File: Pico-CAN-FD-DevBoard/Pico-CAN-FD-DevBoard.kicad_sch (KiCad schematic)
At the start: 2 parts, among them U1 RP2350A, U2 MCP251863T-H-SS

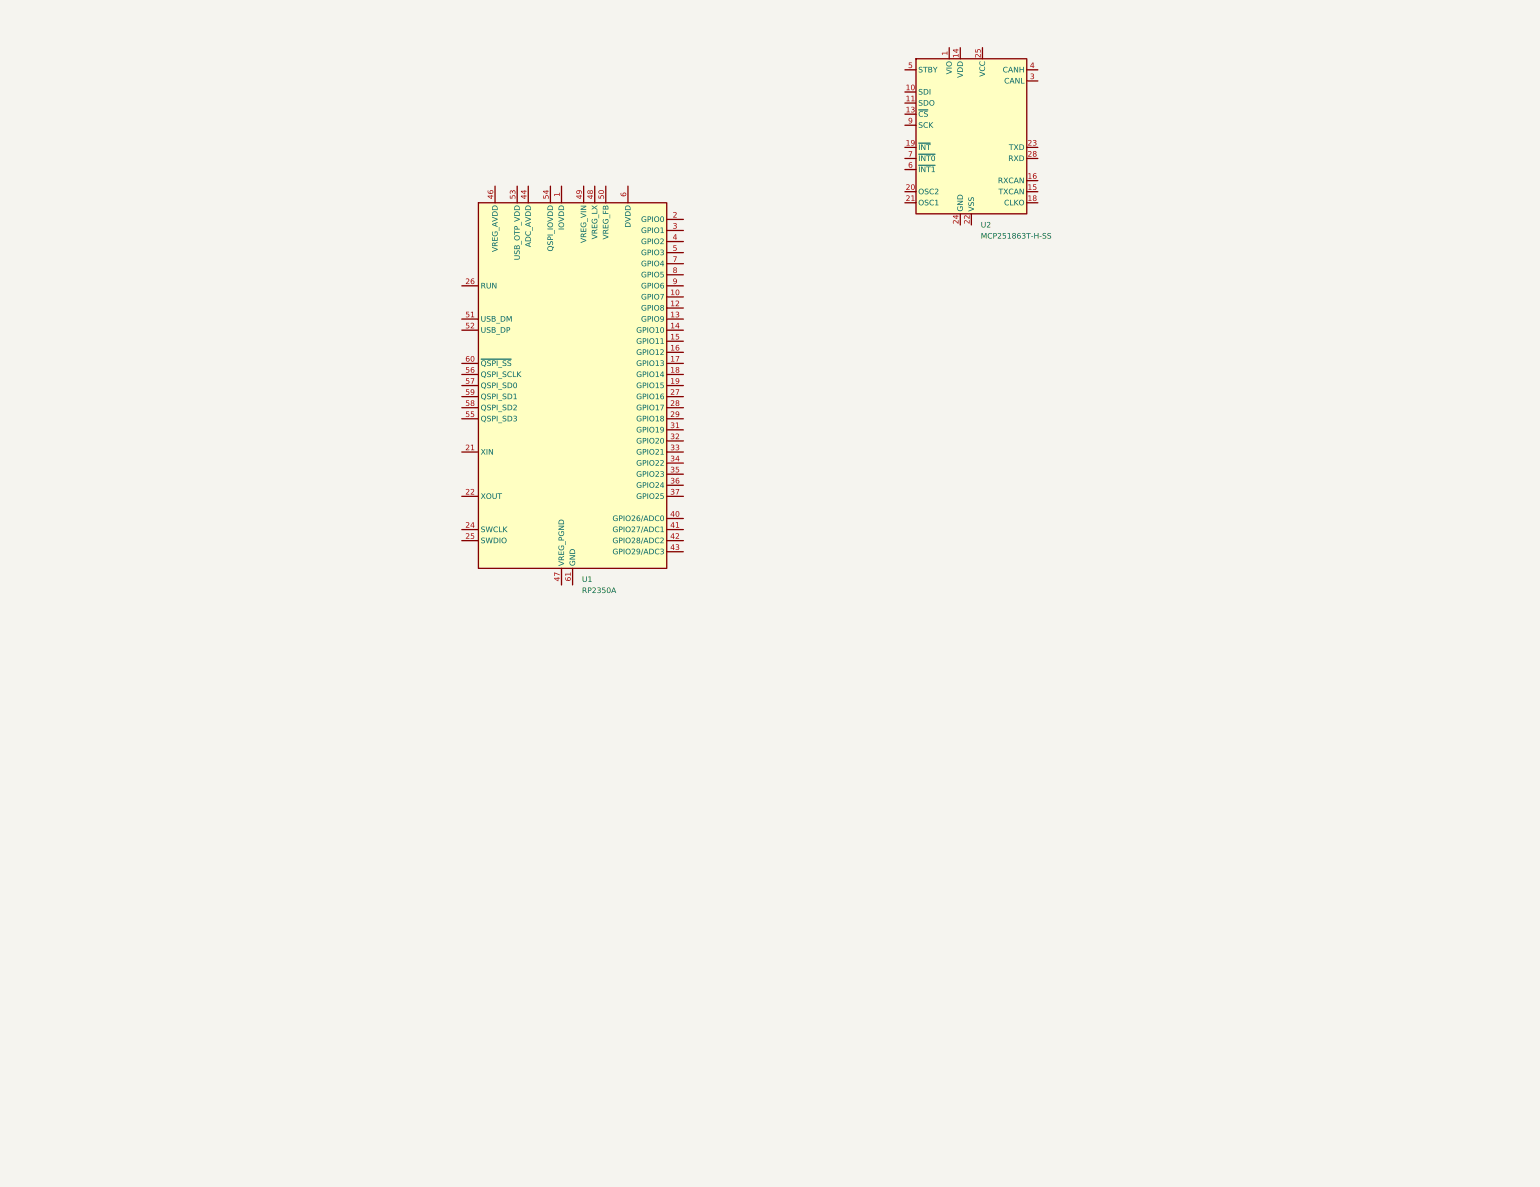
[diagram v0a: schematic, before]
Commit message: added rp2350a and other components
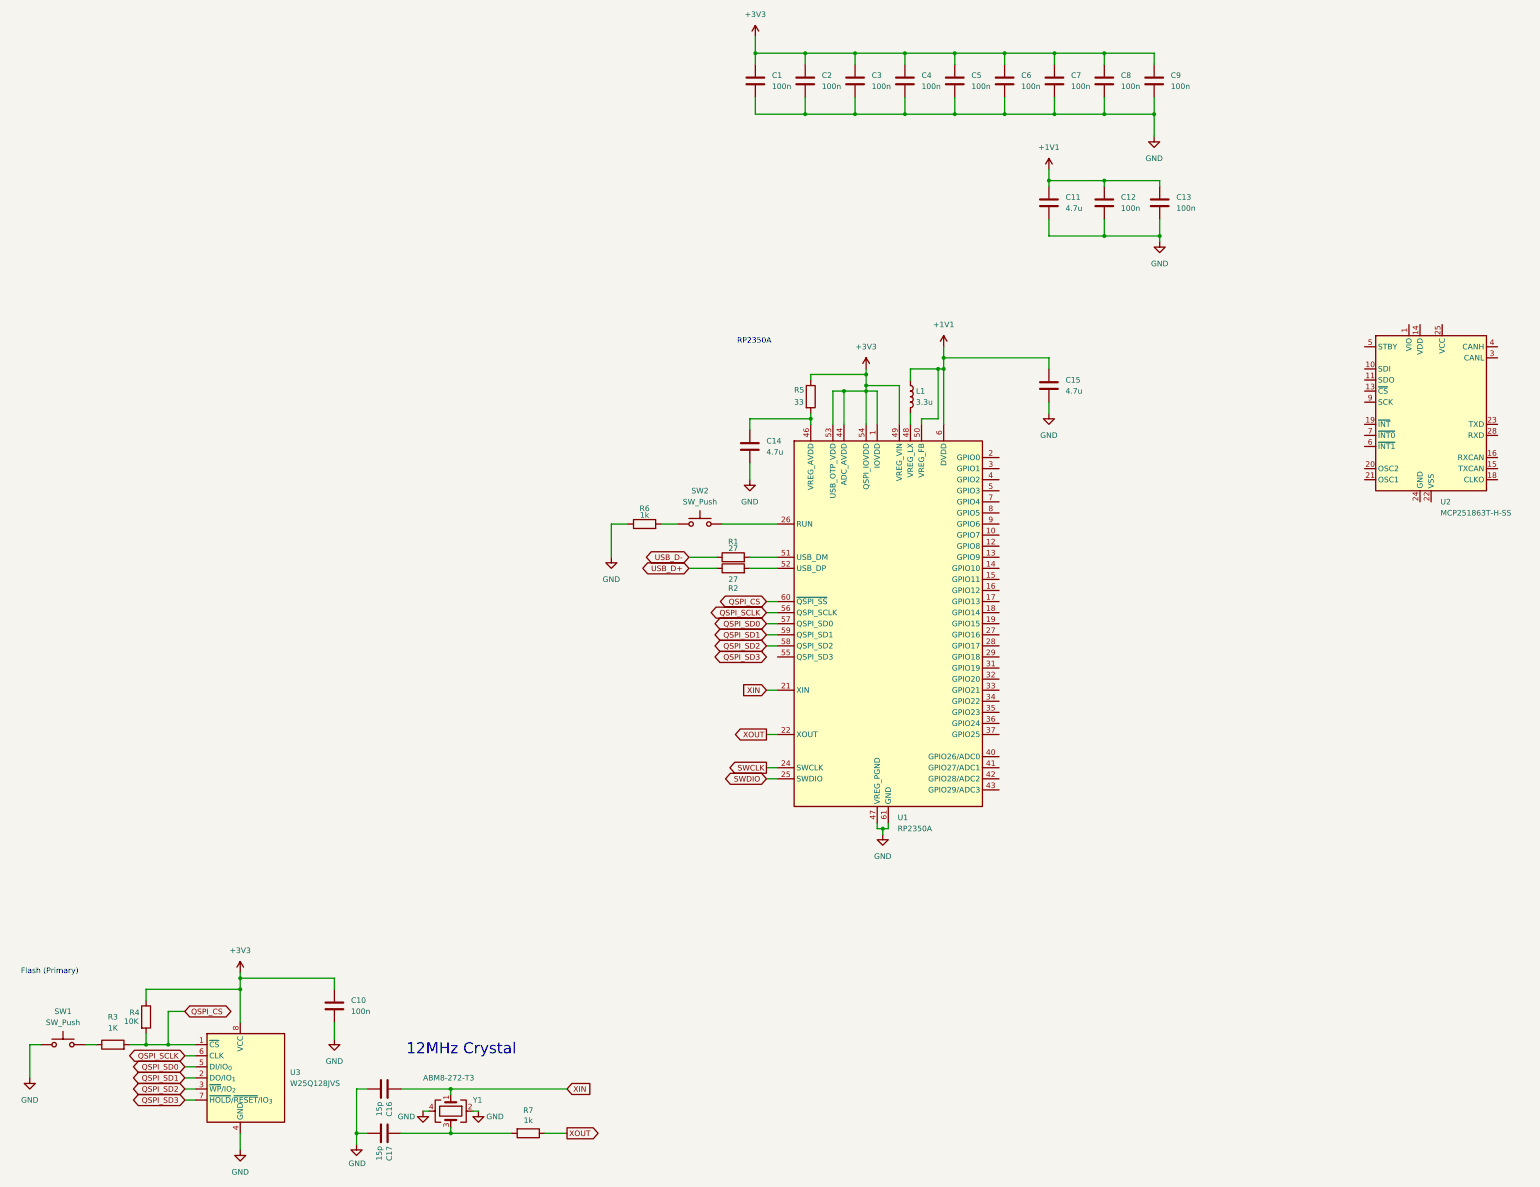
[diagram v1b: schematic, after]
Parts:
- added C1, C10, C12, C13, C2, C3, C4, C5, C6, C7, C8, C9: 100n, symbol Device:C
- added C11, C14, C15: 4.7u, symbol Device:C
- added C16, C17: 15p, Capacitor_SMD:C_0402_1005Metric, symbol Device:C
- added L1: 3.3u, RP2350_60QFN_minimal:L_pol_2016, symbol Device:L
- added R1, R2: 27, symbol Device:R
- added R3: 1K, symbol Device:R
- added R4: 10K, symbol Device:R
- added R5: 33, symbol Device:R
- added R6: 1k, symbol Device:R
- added R7: 1k, Resistor_SMD:R_0402_1005Metric, symbol Device:R
- added SW1, SW2: SW_Push, symbol Switch:SW_Push
- added U3: W25Q128JVS, Package_SO:SOIC-8_5.3x5.3mm_P1.27mm, symbol Memory_Flash:W25Q128JVS
- added Y1: ABM8-272-T3, Crystal:Crystal_SMD_3225-4Pin_3.2x2.5mm, symbol Device:Crystal_GND24
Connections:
- net +3V3: now reaches U1.1 (IOVDD), U1.11 (IOVDD), U1.20 (IOVDD), U1.30 (IOVDD), U1.38 (IOVDD), U1.45 (IOVDD)
- net +3V3: now also U1.44 (ADC_AVDD), U1.49 (VREG_VIN), U1.53 (USB_OTP_VDD), U1.54 (QSPI_IOVDD), C1.1, C10.1, C2.1, C3.1, C4.1, C5.1, C6.1, C7.1, C8.1, C9.1, R4.1, R5.1, U3.8 (VCC)
- net XIN: now reaches U1.21 (XIN)
- net XIN: now also C16.1, Y1.1
- net XOUT: now reaches U1.22 (XOUT)
- net XOUT: now also R7.1
- net +1V1: now reaches U1.23 (DVDD), U1.39 (DVDD), U1.6 (DVDD)
- net +1V1: now also U1.50 (VREG_FB), C11.1, C12.1, C13.1, C15.1, L1.1
- net SWCLK: now reaches U1.24 (SWCLK)
- net SWDIO: now reaches U1.25 (SWDIO)
- net at U1.26 (RUN): now also SW2.2
- net at U1.46 (VREG_AVDD): now also C14.1, R5.2
- net GND: now reaches U1.47 (VREG_PGND)
- net GND: now also U1.61 (GND), C1.2, C10.2, C11.2, C12.2, C13.2, C14.2, C15.2, C16.2, C17.2, C2.2, C3.2, C4.2, C5.2, C6.2, C7.2, C8.2, C9.2, R6.1, SW1.1, U3.4 (GND), Y1.2, Y1.4
- net at U1.48 (VREG_LX): now also L1.2
- net at U1.51 (USB_DM): now also R1.2
- net at U1.52 (USB_DP): now also R2.2
- net QSPI_SCLK: now reaches U1.56 (QSPI_SCLK)
- net QSPI_SCLK: now also U3.6 (CLK)
- net QSPI_SD0: now reaches U1.57 (QSPI_SD0)
- net QSPI_SD0: now also U3.5 (DI/IO_{0})
- net QSPI_SD2: now reaches U1.58 (QSPI_SD2)
- net QSPI_SD2: now also U3.3 (~{WP}/IO_{2})
- net QSPI_SD1: now reaches U1.59 (QSPI_SD1)
- net QSPI_SD1: now also U3.2 (DO/IO_{1})
- net QSPI_CS: now reaches U1.60 (~{QSPI_SS})
- net QSPI_CS: now also R3.2, R4.2, U3.1 (~{CS})
- new net: R3.1, SW1.2
- new net: R6.2, SW2.1
- new net: C17.1, R7.2, Y1.3
- new net QSPI_SD3: U3.7 (~{HOLD}/~{RESET}/IO_{3})
- new net USB_D+: R2.1
- new net USB_D-: R1.1
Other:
- note added: "12MHz Crystal"
- note added: "Flash (Primary)"
- note added: "RP2350A"
- moved on the sheet: U1, U2

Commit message: added more stuff
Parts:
- added C18, C19: 0.1u, symbol Device:C
- added J3: USB_C_Receptacle_USB2.0_14P, symbol Connector:USB_C_Receptacle_USB2.0_14P
- added R8, R9: 5.1k, symbol Device:R
- added U4: SN74HCT125DR, easyeda2kicad:SOIC-14_L8.7-W3.9-P1.27-LS6.0-BL, symbol easyeda2kicad:SN74HCT125DR
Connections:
- net +3V3: now also U2.1 (VIO), U2.14 (VDD), C18.2, C19.2
- net GND: now also U2.22 (VSS), U2.24 (GND), C18.1, C19.1, J3.A1 (GND), J3.A12 (GND), J3.B1 (GND), J3.B12 (GND), J3.S1 (SHIELD), R8.2, R9.2
- net USB_D+: now also J3.A6 (D+), J3.B6 (D+)
- net USB_D-: now also J3.A7 (D-), J3.B7 (D-)
- net CAN_SDI: now reaches U2.10 (SDI)
- net CAN_SDO: now reaches U2.11 (SDO)
- net CAN_CS: now reaches U2.13 (~{CS})
- net +5V: now reaches U2.25 (VCC)
- net CAN_SCK: now reaches U2.9 (SCK)
- new net: J3.B5 (CC2), R9.1
- new net: J3.A5 (CC1), R8.1
- new net VBUS: J3.A4 (VBUS), J3.A9 (VBUS), J3.B4 (VBUS), J3.B9 (VBUS)
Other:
- moved on the sheet: C14, C15, L1, R1, R2, R5, R6, SW2, U1, U2

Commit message: fixed things
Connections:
- net QSPI_SD3: now also U1.55 (QSPI_SD3)
- net QSPI_CS1: now reaches U1.2 (GPIO0)
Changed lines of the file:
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@@
+	(wire
+		(pts
+			(xy 173.99 237.49) (xy 176.53 237.49)
+		)
+		(stroke
+			(width 0)
+			(type default)
+		)
+	)
 	(wire
 		(pts
@@
 		(pts
 			(xy 332.74 85.09) (xy 335.28 85.09)
+		)
+		(stroke
+			(width 0)
+			(type default)
+		)
+	)
+	(wire
+		(pts
+			(xy 227.33 191.77) (xy 241.3 191.77)
 		)
 		(stroke
@@
 			(effects
 				(font
+					(size 1.27 1.27)
+				)
+				(justify left)
+				(hide yes)
+			)
+		)
+	)
+	(global_label "QSPI_CS1"
+		(shape input)
+		(at 241.3 191.77 0)
+		(fields_autoplaced yes)
+		(effects
+			(font
+				(size 1.27 1.27)
+			)
+			(justify left)
+		)
+		(property "Intersheetrefs" "${INTERSHEET_REFS}"
+			(at 253.3566 191.77 0)
+			(effects
+				(font

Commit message: added things
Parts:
- removed U4: SN74HCT125DR, easyeda2kicad:SOIC-14_L8.7-W3.9-P1.27-LS6.0-BL, symbol easyeda2kicad:SN74HCT125DR
- added C20: 100n, symbol Device:C
- added J1: Conn_01x03, Connector_PinHeader_2.54mm:PinHeader_1x03_P2.54mm_Vertical, symbol Connector_Generic:Conn_01x03
- added R10: 1K, symbol Device:R
- added R11: 10K, symbol Device:R
- added SW3: SW_Push, symbol Switch:SW_Push
- added U4: W25Q128JVS, Package_SO:SOIC-8_5.3x5.3mm_P1.27mm, symbol Memory_Flash:W25Q128JVS
- added U5: ESD2CAN24DBZRQ1, easyeda2kicad:SOT-23-3_L2.9-W1.3-P1.90-LS2.4-BR, symbol easyeda2kicad:ESD2CAN24DBZRQ1
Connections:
- net +3V3: now also C20.1, R11.1, U4.8 (VCC)
- net CAN_CS: now also U1.28 (GPIO17)
- net CAN_SCK: now also U1.29 (GPIO18)
- net CAN_SDI: now also U1.27 (GPIO16)
- net CAN_SDO: now also U1.31 (GPIO19)
- net GND: now also C20.2, J1.2 (Pin_2), SW3.1, U4.4 (GND), U5.3 (GND)
- net QSPI_CS1: now also R10.2, R11.2, U4.1 (~{CS})
- net QSPI_SCLK: now also U4.6 (CLK)
- net QSPI_SD0: now also U4.5 (DI/IO_{0})
- net QSPI_SD1: now also U4.2 (DO/IO_{1})
- net QSPI_SD2: now also U4.3 (~{WP}/IO_{2})
- net QSPI_SD3: now also U4.7 (~{HOLD}/~{RESET}/IO_{3})
- net SWCLK: now also J1.1 (Pin_1)
- net SWDIO: now also J1.3 (Pin_3)
- net NPXL_3V3_3: now reaches U1.10 (GPIO7)
- net NPXL_3V3_4: now reaches U1.12 (GPIO8)
- net NPXL_3V3_5: now reaches U1.13 (GPIO9)
- net DS1_DATA: now reaches U1.14 (GPIO10)
- net DS1_CLK: now reaches U1.15 (GPIO11)
- net SPI_SDI: now reaches U1.16 (GPIO12)
- net SPI_CS: now reaches U1.17 (GPIO13)
- net SPI_SCK: now reaches U1.18 (GPIO14)
- net SPI_SDO: now reaches U1.19 (GPIO15)
- net CAN_nINT: now reaches U1.32 (GPIO20)
- net DS2_DATA: now reaches U1.33 (GPIO21)
- net DS2_CLK: now reaches U1.34 (GPIO22)
- net SDA: now reaches U1.4 (GPIO2)
- net SCL: now reaches U1.5 (GPIO3)
- net NPXL_3V3_0: now reaches U1.7 (GPIO4)
- net NPXL_3V3_1: now reaches U1.8 (GPIO5)
- net NPXL_3V3_2: now reaches U1.9 (GPIO6)
- net at U2.3 (CANL): now also U5.2 (IO)
- net at U2.4 (CANH): now also U5.1 (IO)
- new net: R10.1, SW3.2
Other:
- note added: "Decoupling Caps"
- note added: "Flash/PSRAM (Secondary)"
- note added: "SWD Debug"
- note added: "USB-C"
- moved on the sheet: C10, C18, C19, R3, R4, SW1, U2, U3

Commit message: edited things
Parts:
- added J2: Conn_01x08, symbol Connector_Generic:Conn_01x08
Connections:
- net CAN_nINT: now also U2.19 (~{INT})
- net CAN_nINT0: now reaches U1.3 (GPIO1)
- net CAN_nINT0: now also U2.7 (~{INT0})
- net CAN_L: now reaches U2.3 (CANL), U5.2 (IO)
- net CAN_H: now reaches U2.4 (CANH), U5.1 (IO)
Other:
- note added: "CAN-FD"

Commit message: added more things
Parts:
- removed SW3: SW_Push, symbol Switch:SW_Push
- added C21: 0.1u, symbol Device:C
- added C22, C23: 10p, symbol Device:C
- added CN1: SM04B-SRSS-TB (LF)(SN), easyeda2kicad:CONN-SMD_4P-P1.00_SM04B-SRSS-TB-LF-SN, symbol easyeda2kicad:SM04B-SRSS-TB(LF)(SN)
- added R12, R13: 2.2k, symbol Device:R
- added U6: TPS51386RJNR, TPS51386RJNR:VREG_TPS51386RJNR, symbol TPS51386RJNR:TPS51386RJNR
- added Y2: Crystal 40MHz, symbol Device:Crystal
- R10: value 1K -> 4.7k
- U4: now not fitted
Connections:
- net SPI_CS is gone; now on net SPI_RFID_CS: U1.17 (GPIO13)
- net +3V3: now also J2.1 (Pin_1), R10.1, CN1.2, R12.1, R13.1
- net +5V: now also C21.1
- net GND: now also J2.3 (Pin_3), R11.2, U1.2 (GPIO0), U4.1 (~{CS}), C21.2, CN1.1, CN1.5, CN1.6
- net SCL: now also CN1.4, R13.2
- net SDA: now also CN1.3, R12.2
- net SPI_SCK: now also J2.7 (Pin_7)
- net SPI_SDI: now also J2.5 (Pin_5)
- net SPI_SDO: now also J2.6 (Pin_6)
- net at SW2.2, U1.26 (RUN): now also R10.2
- net RFID_RST: now reaches U1.35 (GPIO23)
- net RFID_RST: now also J2.2 (Pin_2)
- net at U2.15 (TXCAN): now also U2.23 (TXD)
- net at U2.16 (RXCAN): now also U2.28 (RXD)
- net at U2.20 (OSC2): now also C22.2
- net at U2.21 (OSC1): now also C23.2
- net CAN_STBY: now reaches U2.5 (STBY)
- net SPI_RFID_CS: now reaches J2.8 (Pin_8)
- removed net QSPI_CS1: R10.2, R11.2, U1.2 (GPIO0), U4.1 (~{CS})
- new net: C23.1, Y2.1
- new net: C22.1, Y2.2
- no-connect marks 0 -> 1
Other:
- note added: "I2C (Qwiic)"
- note added: "SPI RFID/NFC"
- moved on the sheet: C14, C15, J2, L1, R1, R2, R5, R6, SW2, U1
